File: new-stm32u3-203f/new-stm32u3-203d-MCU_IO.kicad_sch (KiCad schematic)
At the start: 7 parts, among them SW1 SW_SPDT, U1 STM32U385RGT6Q, X1 32.768kHz

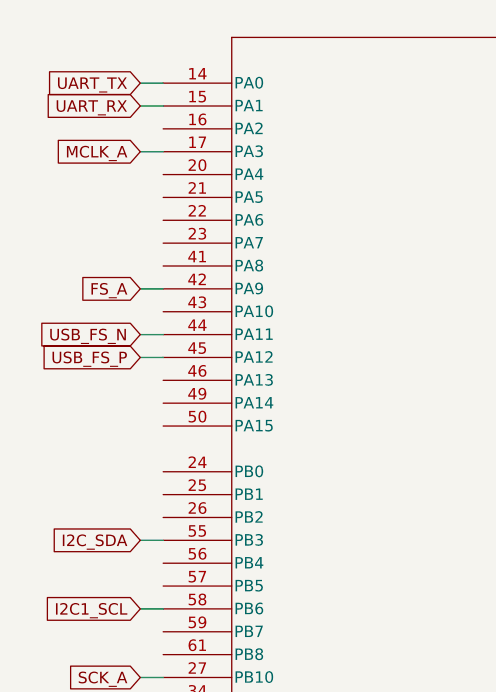
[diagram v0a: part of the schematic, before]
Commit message: added buttons, added uart, added display.
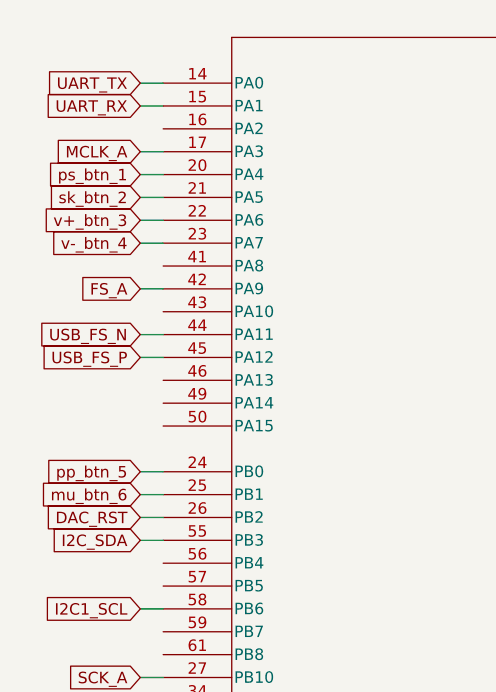
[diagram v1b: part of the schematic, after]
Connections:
- net ps_btn_1: now reaches U1.20 (PA4)
- net sk_btn_2: now reaches U1.21 (PA5)
- net v+_btn_3: now reaches U1.22 (PA6)
- net v-_btn_4: now reaches U1.23 (PA7)
- net pp_btn_5: now reaches U1.24 (PB0)
- net mu_btn_6: now reaches U1.25 (PB1)
- net DAC_RST: now reaches U1.26 (PB2)
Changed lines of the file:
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@@
+	(wire
+		(pts
+			(xy 93.98 55.88) (xy 96.52 55.88)
+		)
+		(stroke
+			(width 0)
+			(type default)
+		)
+	)
 	(wire
 		(pts
@@
 	(wire
 		(pts
+			(xy 93.98 50.8) (xy 96.52 50.8)
+		)
+		(stroke
+			(width 0)
+			(type default)
+		)
+	)
+	(wire
+		(pts
 			(xy 157.48 58.42) (xy 160.02 58.42)
 		)
@@
 	(wire
 		(pts
+			(xy 93.98 48.26) (xy 96.52 48.26)
+		)
+		(stroke
+			(width 0)
+			(type default)
+		)
+	)
+	(wire
+		(pts
 			(xy 93.98 45.72) (xy 96.52 45.72)
 		)
@@
 	(wire
 		(pts
+			(xy 93.98 86.36) (xy 96.52 86.36)
+		)
+		(stroke
+			(width 0)
+			(type default)
+		)
+	)
+	(wire
+		(pts
 			(xy 157.48 40.64) (xy 160.02 40.64)
 		)
@@
 	(wire
 		(pts
+			(xy 93.98 53.34) (xy 96.52 53.34)
+		)
+		(stroke
+			(width 0)
+			(type default)
+		)
+	)
+	(wire
+		(pts
+			(xy 93.98 83.82) (xy 96.52 83.82)
+		)
+		(stroke
+			(width 0)
+			(type default)
+		)
+	)
+	(wire
+		(pts
 			(xy 157.48 91.44) (xy 163.83 91.44)
 		)
@@
 		(pts
 			(xy 157.48 55.88) (xy 160.02 55.88)
+		)
+		(stroke
+			(width 0)
+			(type default)
+		)
+	)
+	(wire
+		(pts
+			(xy 93.98 81.28) (xy 96.52 81.28)
 		)
 		(stroke
@@
 		)
 	)
+	(global_label "mu_btn_6"
+		(shape input)
+		(at 93.98 83.82 180)
+		(fields_autoplaced yes)
+		(effects
+			(font
+				(size 1.27 1.27)
+			)
+			(justify right)
+		)
+		(property "Intersheetrefs" "${INTERSHEET_REFS}"
+			(at 81.9841 83.82 0)
+			(effects
+				(font
+					(size 1.27 1.27)
+				)
+				(justify right)
+				(hide yes)
+			)
+		)
+	)
+	(global_label "sk_btn_2"
+		(shape input)
+		(at 93.98 50.8 180)
+		(fields_autoplaced yes)
+		(effects
+			(font
+				(size 1.27 1.27)
+			)
+			(justify right)
+		)
+		(property "Intersheetrefs" "${INTERSHEET_REFS}"
+			(at 82.7702 50.8 0)
+			(effects
+				(font
+					(size 1.27 1.27)
+				)
+				(justify right)
+				(hide yes)
+			)
+		)
+	)
 	(global_label "SD_DAT1"
 		(shape input)
@@
 		)
 	)
+	(global_label "ps_btn_1"
+		(shape input)
+		(at 93.98 48.26 180)
+		(fields_autoplaced yes)
+		(effects
+			(font
+				(size 1.27 1.27)
+			)
+			(justify right)
+		)
+		(property "Intersheetrefs" "${INTERSHEET_REFS}"
+			(at 82.6493 48.26 0)
+			(effects
+				(font
+					(size 1.27 1.27)
+				)
+				(justify right)
+				(hide yes)
+			)
+		)
+	)
 	(global_label "SD_CMD"
 		(shape input)
@@
 		)
 	)
+	(global_label "DAC_RST"
+		(shape input)
+		(at 93.98 86.36 180)
+		(fields_autoplaced yes)
+		(effects
+			(font
+				(size 1.27 1.27)
+			)
+			(justify right)
+		)
+		(property "Intersheetrefs" "${INTERSHEET_REFS}"
+			(at 82.9515 86.36 0)
+			(effects
+				(font
+					(size 1.27 1.27)
+				)
+				(justify right)
+				(hide yes)
+			)
+		)
+	)
+	(global_label "v+_btn_3"
+		(shape input)
+		(at 93.98 53.34 180)
+		(fields_autoplaced yes)
+		(effects
+			(font
+				(size 1.27 1.27)
+			)
+			(justify right)
+		)
+		(property "Intersheetrefs" "${INTERSHEET_REFS}"
+			(at 82.2864 53.34 0)
+			(effects
+				(font
+					(size 1.27 1.27)
+				)
+				(justify right)
+				(hide yes)
+			)
+		)
+	)
 	(global_label "USB_FS_P"
 		(shape input)
@@
 		)
 	)
+	(global_label "v-_btn_4"
+		(shape input)
+		(at 93.98 55.88 180)
+		(fields_autoplaced yes)
+		(effects
+			(font
+				(size 1.27 1.27)
+			)
+			(justify right)
+		)
+		(property "Intersheetrefs" "${INTERSHEET_REFS}"
+			(at 82.2864 55.88 0)
+			(effects
+				(font
+					(size 1.27 1.27)
+				)
+				(justify right)
+				(hide yes)
+			)
+		)
+	)
 	(global_label "OSC_OUT"
 		(shape input)
@@
 			(effects
 				(font
+					(size 1.27 1.27)
+				)
+				(justify right)
+				(hide yes)
+			)
+		)
+	)
+	(global_label "pp_btn_5"
+		(shape input)
+		(at 93.98 81.28 180)
+		(fields_autoplaced yes)
+		(effects
+			(font
+				(size 1.27 1.27)
+			)
+			(justify right)
+		)
+		(property "Intersheetrefs" "${INTERSHEET_REFS}"
+			(at 82.5284 81.28 0)
+			(effects
+				(font

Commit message: finished the schematic, just need someone to review it :)
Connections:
- no-connect marks 0 -> 21
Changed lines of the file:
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@@
 		(color 0 0 0 0)
+	)
+	(no_connect
+		(at 157.48 50.8)
+	)
+	(no_connect
+		(at 96.52 58.42)
+	)
+	(no_connect
+		(at 96.52 76.2)
+	)
+	(no_connect
+		(at 157.48 48.26)
+	)
+	(no_connect
+		(at 96.52 101.6)
+	)
+	(no_connect
+		(at 157.48 45.72)
+	)
+	(no_connect
+		(at 157.48 66.04)
+	)
+	(no_connect
+		(at 96.52 71.12)
+	)
+	(no_connect
+		(at 96.52 43.18)
+	)
+	(no_connect
+		(at 96.52 93.98)
+	)
+	(no_connect
+		(at 157.48 83.82)
+	)
+	(no_connect
+		(at 96.52 109.22)
+	)
+	(no_connect
+		(at 157.48 81.28)
+	)
+	(no_connect
+		(at 96.52 63.5)
+	)
+	(no_connect
+		(at 96.52 73.66)
+	)
+	(no_connect
+		(at 157.48 38.1)
+	)
+	(no_connect
+		(at 96.52 91.44)
+	)
+	(no_connect
+		(at 96.52 106.68)
+	)
+	(no_connect
+		(at 96.52 111.76)
+	)
+	(no_connect
+		(at 157.48 43.18)
+	)
+	(no_connect
+		(at 96.52 99.06)
 	)
 	(wire

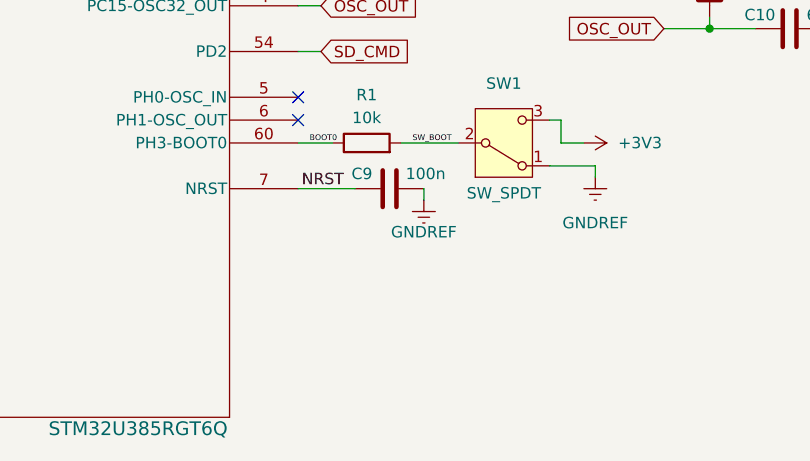
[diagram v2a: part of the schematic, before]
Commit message: added reset button. asigned footprints.
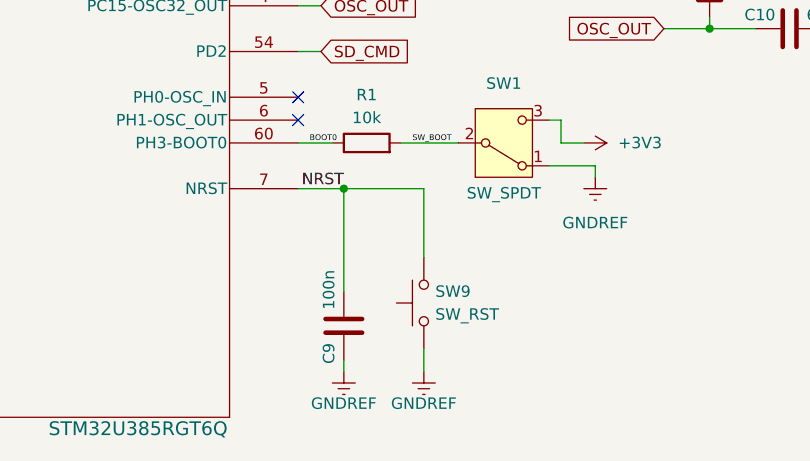
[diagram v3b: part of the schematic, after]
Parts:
- added SW9: SW_RST, footprints_RST_BTN:SON4_PTS526 SM15 SMTR2 LFS_CNK, symbol Switch:SW_Push
- C10, C11, C9: footprint (none) -> Capacitor_SMD:C_0603_1608Metric
- R1: footprint (none) -> Resistor_SMD:R_0603_1608Metric
- SW1: footprint (none) -> footprints_SPDT_slide:CL-SB-12B-01_NDC
- U1: footprint LQFP64_STM -> Package_QFP:LQFP-64_10x10mm_P0.5mm
- X1: footprint (none) -> Crystal:Crystal_SMD_3215-2Pin_3.2x1.5mm
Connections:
- net GNDREF: now also C9.1, SW9.1; no longer C9.2
- net NRST: now also C9.2, SW9.2; no longer C9.1
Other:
- moved on the sheet: C9
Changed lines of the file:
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@@
 	(paper "A4")
+	(junction
+		(at 162.56 91.44)
+		(diameter 0)
+		(color 0 0 0 0)
+	)
 	(junction
 		(at 203.2 73.66)
@@
 	(wire
 		(pts
+			(xy 171.45 99.06) (xy 171.45 91.44)
+		)
+		(stroke
+			(width 0)
+			(type default)
+		)
+	)
+	(wire
+		(pts
 			(xy 157.48 60.96) (xy 160.02 60.96)
 		)
@@
 	(wire
 		(pts
-			(xy 171.45 92.71) (xy 171.45 91.44)
+			(xy 162.56 111.76) (xy 162.56 110.49)
 		)
 		(stroke
@@
 	(wire
 		(pts
+			(xy 171.45 109.22) (xy 171.45 111.76)
+		)
+		(stroke
+			(width 0)
+			(type default)
+		)
+	)
+	(wire
+		(pts
 			(xy 93.98 48.26) (xy 96.52 48.26)
 		)
@@
 	(wire
 		(pts
-			(xy 157.48 91.44) (xy 163.83 91.44)
-		)
-		(stroke
-			(width 0)
-			(type default)
-		)
-	)
-	(wire
-		(pts
 			(xy 93.98 38.1) (xy 96.52 38.1)
 		)
@@
 		(pts
 			(xy 190.5 88.9) (xy 190.5 90.17)
+		)
+		(stroke
+			(width 0)
+			(type default)
+		)
+	)
+	(wire
+		(pts
+			(xy 162.56 91.44) (xy 157.48 91.44)
+		)
+		(stroke
+			(width 0)
+			(type default)
+		)
+	)
+	(wire
+		(pts
+			(xy 162.56 91.44) (xy 162.56 102.87)
+		)
+		(stroke
+			(width 0)
+			(type default)
+		)
+	)
+	(wire
+		(pts
+			(xy 171.45 91.44) (xy 162.56 91.44)
 		)
 		(stroke
@@
 			)
 		)
-		(property "Footprint" ""
+		(property "Footprint" "Crystal:Crystal_SMD_3215-2Pin_3.2x1.5mm"
 			(at 203.2 68.58 0)
 			(effects
@@
 				(path "/133609ce-1e1a-4c9a-bce3-37a0219dc965/2a65a93f-e384-446c-b635-357d5c94d301"
 					(reference "X1")
+					(unit 1)
+				)
+			)
+		)
+	)
+	(symbol
+		(lib_id "power:GNDREF")
+		(at 171.45 111.76 0)
+		(unit 1)
+		(exclude_from_sim no)
+		(in_bom yes)
+		(on_board yes)
+		(dnp no)
+		(property "Reference" "#PWR069"
+			(at 171.45 118.11 0)
+			(effects
+				(font
+					(size 1.27 1.27)
+				)
+				(hide yes)
+			)
+		)
+		(property "Value" "GNDREF"
+			(at 171.45 115.316 0)
+			(effects
+				(font
+					(size 1.27 1.27)
+				)
+			)
+		)
+		(property "Footprint" ""
+			(at 171.45 111.76 0)
+			(effects
+				(font
+					(size 1.27 1.27)
+				)
+				(hide yes)
+			)
+		)
+		(property "Datasheet" ""
+			(at 171.45 111.76 0)
+			(effects
+				(font
+					(size 1.27 1.27)
+				)
+				(hide yes)
+			)
+		)
+		(property "Description" "Power symbol creates a global label with name \"GNDREF\" , reference supply ground"
+			(at 171.45 111.76 0)
+			(effects
+				(font
+					(size 1.27 1.27)
+				)
+				(hide yes)
+			)
+		)
+		(pin "1"
+		)
+		(instances
+			(project "new-stm32u3-203f"
+				(path "/133609ce-1e1a-4c9a-bce3-37a0219dc965/2a65a93f-e384-446c-b635-357d5c94d301"
+					(reference "#PWR069")
 					(unit 1)
 				)
@@
 			)
 		)
-		(property "Footprint" ""
+		(property "Footprint" "footprints_SPDT_slide:CL-SB-12B-01_NDC"
 			(at 180.34 86.36 0)
 			(effects
@@
 	(symbol
 		(lib_id "power:GNDREF")
-		(at 171.45 92.71 0)
+		(at 162.56 111.76 0)
 		(unit 1)
 		(exclude_from_sim no)
@@
 		(dnp no)
 		(property "Reference" "#PWR010"
-			(at 171.45 99.06 0)
+			(at 162.56 118.11 0)
 			(effects
 				(font
@@
 		)
 		(property "Value" "GNDREF"
-			(at 171.45 96.266 0)
+			(at 162.56 115.316 0)
 			(effects
 				(font
@@
 		)
 		(property "Footprint" ""
-			(at 171.45 92.71 0)
+			(at 162.56 111.76 0)
 			(effects
 				(font
@@
 		)
 		(property "Datasheet" ""
-			(at 171.45 92.71 0)
+			(at 162.56 111.76 0)
 			(effects
 				(font
@@
 		)
 		(property "Description" "Power symbol creates a global label with name \"GNDREF\" , reference supply ground"
-			(at 171.45 92.71 0)
+			(at 162.56 111.76 0)
 			(effects
 				(font
@@
 	(symbol
 		(lib_id "Device:C")
-		(at 167.64 91.44 90)
+		(at 162.56 106.68 180)
 		(unit 1)
 		(exclude_from_sim no)
@@
 		(dnp no)
 		(property "Reference" "C9"
-			(at 165.735 89.789 90)
+			(at 160.909 108.585 90)
 			(effects
 				(font
@@
 		)
 		(property "Value" "100n"
-			(at 173.863 89.789 90)
+			(at 160.909 100.457 90)
 			(effects
 				(font
@@
 			)
 		)
-		(property "Footprint" ""
-			(at 171.45 90.4748 0)
+		(property "Footprint" "Capacitor_SMD:C_0603_1608Metric"
+			(at 161.5948 102.87 0)
 			(effects
 				(font
@@
 		)
 		(property "Datasheet" "~"
-			(at 167.64 91.44 0)
+			(at 162.56 106.68 0)
 			(effects
 				(font
@@
 		)
 		(property "Description" "Unpolarized capacitor"
-			(at 167.64 91.44 0)
+			(at 162.56 106.68 0)
 			(effects
 				(font
@@
 			)
 		)
-		(property "Footprint" ""
+		(property "Footprint" "Capacitor_SMD:C_0603_1608Metric"
 			(at 215.9 62.5348 0)
 			(effects
@@
 			)
 		)
-		(property "Footprint" "LQFP64_STM"
+		(property "Footprint" "Package_QFP:LQFP-64_10x10mm_P0.5mm"
 			(at 96.52 38.1 0)
 			(effects
@@
 			)
 		)
-		(property "Footprint" ""
+		(property "Footprint" "Capacitor_SMD:C_0603_1608Metric"
 			(at 215.9 72.6948 0)
 			(effects
@@
 			)
 		)
-		(property "Footprint" ""
+		(property "Footprint" "Resistor_SMD:R_0603_1608Metric"
 			(at 165.1 88.138 90)
 			(effects
@@
 					(unit 1)
 				)
+			)
+		)
+	)
+	(symbol
+		(lib_id "Switch:SW_Push")
+		(at 171.45 104.14 90)
+		(unit 1)
+		(exclude_from_sim no)
+		(in_bom yes)
+		(on_board yes)
+		(dnp no)
+		(fields_autoplaced yes)
+		(property "Reference" "SW9"
+			(at 172.72 102.8699 90)
+			(effects
+				(font
+					(size 1.27 1.27)
+				)
+				(justify right)
+			)
+		)
+		(property "Value" "SW_RST"
+			(at 172.72 105.4099 90)
+			(effects
+				(font
+					(size 1.27 1.27)
+				)
+				(justify right)
+			)
+		)
+		(property "Footprint" "footprints_RST_BTN:SON4_PTS526 SM15 SMTR2 LFS_CNK"
+			(at 166.37 104.14 0)
+			(effects
+				(font
+					(size 1.27 1.27)
+				)
+				(hide yes)
+			)
+		)
+		(property "Datasheet" "~"
+			(at 166.37 104.14 0)
+			(effects
+				(font
+					(size 1.27 1.27)
+				)
+				(hide yes)
+			)
+		)
+		(property "Description" "Push button switch, generic, two pins"
+			(at 171.45 104.14 0)
+			(effects
+				(font
+					(size 1.27 1.27)
+				)
+				(hide yes)
+			)
+		)
+		(pin "2"
+		)
+		(pin "1"
+		)
+		(instances
+			(project ""
+				(path "/133609ce-1e1a-4c9a-bce3-37a0219dc965/2a65a93f-e384-446c-b635-357d5c94d301"
+					(reference "SW9")
+					(unit 1)
+				)

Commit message: made some progress on the pcb
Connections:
- net mu_btn_6: no longer names the net of U1.25 (PB1)
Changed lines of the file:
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@@
-		)
-	)
-	(global_label "mu_btn_6"
-		(shape input)
-		(at 93.98 83.82 180)
-		(fields_autoplaced yes)
-		(effects
-			(font
-				(size 1.27 1.27)
-			)
-			(justify right)
-		)
-		(property "Intersheetrefs" "${INTERSHEET_REFS}"
-			(at 81.9841 83.82 0)
-			(effects
-				(font
-					(size 1.27 1.27)
-				)
-				(justify right)
-				(hide yes)
-			)
 		)
 	)

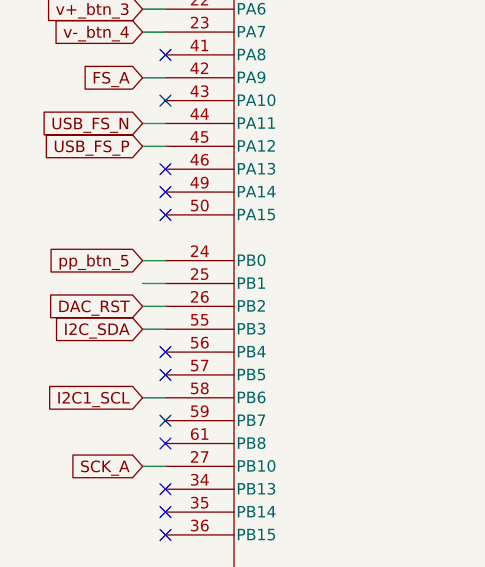
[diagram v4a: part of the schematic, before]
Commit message: moved over to just using direct usb 2.0, made progress on pcb layout
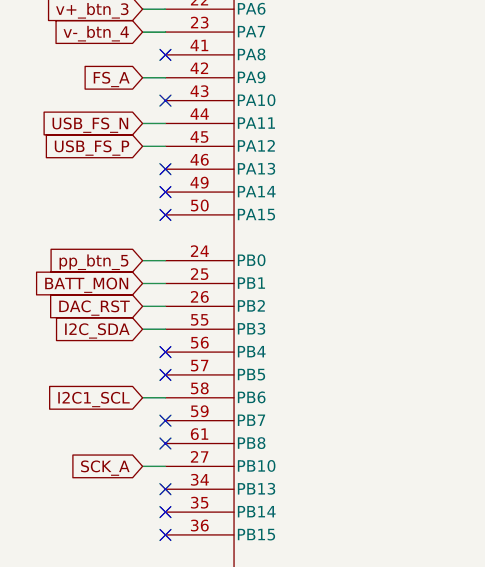
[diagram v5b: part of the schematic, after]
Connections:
- net BATT_MON: now reaches U1.25 (PB1)
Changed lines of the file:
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@@
+		)
+	)
+	(global_label "BATT_MON"
+		(shape input)
+		(at 93.98 83.82 180)
+		(fields_autoplaced yes)
+		(effects
+			(font
+				(size 1.27 1.27)
+			)
+			(justify right)
+		)
+		(property "Intersheetrefs" "${INTERSHEET_REFS}"
+			(at 81.621 83.82 0)
+			(effects
+				(font
+					(size 1.27 1.27)
+				)
+				(justify right)
+				(hide yes)
+			)
 		)
 	)

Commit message: finished the layout of the pcb
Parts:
- SW1: footprint footprints_SPDT_slide:CL-SB-12B-01_NDC -> switch:SW_CJS-1200TA
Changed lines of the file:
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@@
 			)
 		)
-		(property "Footprint" "footprints_SPDT_slide:CL-SB-12B-01_NDC"
+		(property "Footprint" "switch:SW_CJS-1200TA"
 			(at 180.34 86.36 0)
 			(effects

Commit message: made some better progress routing
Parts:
- removed SW9: SW_RST, footprints_RST_BTN:SON4_PTS526 SM15 SMTR2 LFS_CNK, symbol Switch:SW_Push
- added J7: RESET, Connector_PinHeader_1.00mm:PinHeader_1x02_P1.00mm_Vertical, symbol Connector:Conn_01x02_Pin
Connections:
- net GNDREF: now also J7.1 (Pin_1)
- net NRST: now also J7.2 (Pin_2)
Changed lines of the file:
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@@
 	(wire
 		(pts
-			(xy 171.45 99.06) (xy 171.45 91.44)
+			(xy 171.45 91.44) (xy 171.45 102.87)
 		)
 		(stroke
@@
 	(wire
 		(pts
+			(xy 171.45 102.87) (xy 173.99 102.87)
+		)
+		(stroke
+			(width 0)
+			(type default)
+		)
+	)
+	(wire
+		(pts
 			(xy 157.48 68.58) (xy 160.02 68.58)
 		)
@@
 	(wire
 		(pts
-			(xy 171.45 109.22) (xy 171.45 111.76)
+			(xy 171.45 105.41) (xy 171.45 111.76)
 		)
 		(stroke
@@
 		(pts
 			(xy 186.69 86.36) (xy 186.69 83.82)
+		)
+		(stroke
+			(width 0)
+			(type default)
+		)
+	)
+	(wire
+		(pts
+			(xy 173.99 105.41) (xy 171.45 105.41)
 		)
 		(stroke
@@
 	)
 	(symbol
+		(lib_id "Connector:Conn_01x02_Pin")
+		(at 179.07 105.41 180)
+		(unit 1)
+		(exclude_from_sim no)
+		(in_bom yes)
+		(on_board yes)
+		(dnp no)
+		(property "Reference" "J7"
+			(at 178.054 97.282 0)
+			(effects
+				(font
+					(size 1.27 1.27)
+				)
+			)
+		)
+		(property "Value" "RESET"
+			(at 177.8 99.568 0)
+			(effects
+				(font
+					(size 1.27 1.27)
+				)
+			)
+		)
+		(property "Footprint" "Connector_PinHeader_1.00mm:PinHeader_1x02_P1.00mm_Vertical"
+			(at 179.07 105.41 0)
+			(effects
+				(font
+					(size 1.27 1.27)
+				)
+				(hide yes)
+			)
+		)
+		(property "Datasheet" "~"
+			(at 179.07 105.41 0)
+			(effects
+				(font
+					(size 1.27 1.27)
+				)
+				(hide yes)
+			)
+		)
+		(property "Description" "Generic connector, single row, 01x02, script generated"
+			(at 179.07 105.41 0)
+			(effects
+				(font
+					(size 1.27 1.27)
+				)
+				(hide yes)
+			)
+		)
+		(pin "2"
+		)
+		(pin "1"
+		)
+		(instances
+			(project "new-stm32u3-203f"
+				(path "/133609ce-1e1a-4c9a-bce3-37a0219dc965/2a65a93f-e384-446c-b635-357d5c94d301"
+					(reference "J7")
+					(unit 1)
+				)
+			)
+		)
+	)
+	(symbol
 		(lib_id "power:GNDREF")
 		(at 219.71 63.5 0)
@@
 					(unit 1)
 				)
-			)
-		)
-	)
-	(symbol
-		(lib_id "Switch:SW_Push")
-		(at 171.45 104.14 90)
-		(unit 1)
-		(exclude_from_sim no)
-		(in_bom yes)
-		(on_board yes)
-		(dnp no)
-		(fields_autoplaced yes)
-		(property "Reference" "SW9"
-			(at 172.72 102.8699 90)
-			(effects
-				(font
-					(size 1.27 1.27)
-				)
-				(justify right)
-			)
-		)
-		(property "Value" "SW_RST"
-			(at 172.72 105.4099 90)
-			(effects
-				(font
-					(size 1.27 1.27)
-				)
-				(justify right)
-			)
-		)
-		(property "Footprint" "footprints_RST_BTN:SON4_PTS526 SM15 SMTR2 LFS_CNK"
-			(at 166.37 104.14 0)
-			(effects
-				(font
-					(size 1.27 1.27)
-				)
-				(hide yes)
-			)
-		)
-		(property "Datasheet" "~"
-			(at 166.37 104.14 0)
-			(effects
-				(font
-					(size 1.27 1.27)
-				)
-				(hide yes)
-			)
-		)
-		(property "Description" "Push button switch, generic, two pins"
-			(at 171.45 104.14 0)
-			(effects
-				(font
-					(size 1.27 1.27)
-				)
-				(hide yes)
-			)
-		)
-		(pin "2"
-		)
-		(pin "1"
-		)
-		(instances
-			(project ""
-				(path "/133609ce-1e1a-4c9a-bce3-37a0219dc965/2a65a93f-e384-446c-b635-357d5c94d301"
-					(reference "SW9")
-					(unit 1)
-				)
